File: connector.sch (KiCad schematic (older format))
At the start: 1 part, among them P3 CONN_01X06

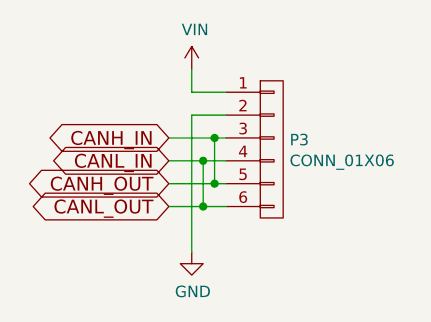
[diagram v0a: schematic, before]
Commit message: Use LMR16006 DCDC
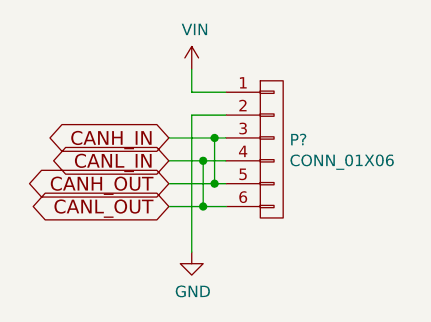
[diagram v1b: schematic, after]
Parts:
- renumbered P3 to P?
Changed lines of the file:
@@
 $EndDescr
 $Comp
-L CONN_01X06 P3
+L CONN_01X06 P?
 U 1 1 57AF467D
 P 3400 4150
-F 0 "P3" H 3478 4191 50  0000 L CNN
+F 0 "P?" H 3478 4191 50  0000 L CNN
 F 1 "CONN_01X06" H 3478 4100 50  0000 L CNN
 F 2 "" H 3400 4150 50  0001 C CNN
@@
 $EndComp
 $Comp
-L VIN #PWR062
+L VIN #PWR?
 U 1 1 57AF4ABC
 P 3050 3800
-F 0 "#PWR062" H 3050 3650 50  0001 C CNN
+F 0 "#PWR?" H 3050 3650 50  0001 C CNN
 F 1 "VIN" H 3065 3973 50  0000 C CNN
 F 2 "" H 3050 3800 60  0000 C CNN
@@
 	3050 3900 3050 3800
 $Comp
-L GND #PWR063
+L GND #PWR?
 U 1 1 57AF4B0E
 P 3050 4600
-F 0 "#PWR063" H 3050 4350 50  0001 C CNN
+F 0 "#PWR?" H 3050 4350 50  0001 C CNN
 F 1 "GND" H 3055 4427 50  0000 C CNN
 F 2 "" H 3050 4600 50  0000 C CNN

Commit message: .
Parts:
- P3: renamed from P?; footprint (none) -> Terminal_Blocks:TerminalBlock_WAGO-236_2Stift_RM5mm_6pol
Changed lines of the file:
@@
 $EndDescr
 $Comp
-L CONN_01X06 P?
+L CONN_01X06 P3
 U 1 1 57AF467D
 P 3400 4150
-F 0 "P?" H 3478 4191 50  0000 L CNN
+F 0 "P3" H 3478 4191 50  0000 L CNN
 F 1 "CONN_01X06" H 3478 4100 50  0000 L CNN
-F 2 "" H 3400 4150 50  0001 C CNN
+F 2 "Terminal_Blocks:TerminalBlock_WAGO-236_2Stift_RM5mm_6pol" H 3400 4150 50  0001 C CNN
 F 3 "" H 3400 4150 50  0000 C CNN
 	1    3400 4150
@@
 $EndComp
 $Comp
-L VIN #PWR?
+L VIN #PWR062
 U 1 1 57AF4ABC
 P 3050 3800
-F 0 "#PWR?" H 3050 3650 50  0001 C CNN
+F 0 "#PWR062" H 3050 3650 50  0001 C CNN
 F 1 "VIN" H 3065 3973 50  0000 C CNN
 F 2 "" H 3050 3800 60  0000 C CNN
@@
 	3050 3900 3050 3800
 $Comp
-L GND #PWR?
+L GND #PWR063
 U 1 1 57AF4B0E
 P 3050 4600
-F 0 "#PWR?" H 3050 4350 50  0001 C CNN
+F 0 "#PWR063" H 3050 4350 50  0001 C CNN
 F 1 "GND" H 3055 4427 50  0000 C CNN
 F 2 "" H 3050 4600 50  0000 C CNN

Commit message: Add bom, minor changes
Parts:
- P3: footprint Terminal_Blocks:TerminalBlock_WAGO-236_2Stift_RM5mm_6pol -> (none)
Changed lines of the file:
@@
 F 0 "P3" H 3478 4191 50  0000 L CNN
 F 1 "CONN_01X06" H 3478 4100 50  0000 L CNN
-F 2 "Terminal_Blocks:TerminalBlock_WAGO-236_2Stift_RM5mm_6pol" H 3400 4150 50  0001 C CNN
+F 2 "" H 3400 4150 50  0001 C CNN
 F 3 "" H 3400 4150 50  0000 C CNN
 	1    3400 4150
